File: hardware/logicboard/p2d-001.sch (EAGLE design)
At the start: 64 parts, among them IC1 74LS06N, IC2 4066N, IC3 MAX3468CPA, J1 MKR, J2 GPIO, J3 Vcc, J4 RLY, J5 SPI, K1 G5V1, T1 2SC1815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

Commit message: Fixed silk and wiring.
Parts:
- RN4: value (none) -> 220
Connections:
- removed net MI: IC1A.I, JP3.3, OK1A.VO1
- net MIN: now also IC1A.I, JP3.3, OK1A.VO1
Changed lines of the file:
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@@
 <part name="SUPPLY14" library="supply2" deviceset="GND" device=""/>
 <part name="IC1" library="74xx-us" library_urn="urn:adsk.eagle:library:88" deviceset="74*06" device="N" package3d_urn="urn:adsk.eagle:package:16407/2" technology="LS"/>
-<part name="RN4" library="resistor-dil" library_urn="urn:adsk.eagle:library:342" deviceset="8R-N" device="" package3d_urn="urn:adsk.eagle:package:922/2"/>
+<part name="RN4" library="resistor-dil" library_urn="urn:adsk.eagle:library:342" deviceset="8R-N" device="" package3d_urn="urn:adsk.eagle:package:922/2" value="220"/>
 <part name="D3" library="SparkFun-DiscreteSemi" library_urn="urn:adsk.eagle:library:514" deviceset="DIODE" device="-1N4148" package3d_urn="urn:adsk.eagle:package:38452/1" value=""/>
 <part name="RN2" library="resistor-net" library_urn="urn:adsk.eagle:library:343" deviceset="RN04" device="" package3d_urn="urn:adsk.eagle:package:24976/1" value="4.7k"/>
@@
 <label x="251.46" y="149.86" size="0.8128" layer="95" xref="yes"/>
 </segment>
+<segment>
+<pinref part="OK1" gate="A" pin="VO1"/>
+<wire x1="167.64" y1="119.38" x2="149.86" y2="119.38" width="0.1524" layer="91"/>
+<label x="147.32" y="119.38" size="0.8128" layer="95" rot="R180" xref="yes"/>
+<pinref part="IC1" gate="A" pin="I"/>
+<wire x1="149.86" y1="119.38" x2="147.32" y2="119.38" width="0.1524" layer="91"/>
+<wire x1="152.4" y1="101.6" x2="149.86" y2="101.6" width="0.1524" layer="91"/>
+<wire x1="149.86" y1="101.6" x2="149.86" y2="119.38" width="0.1524" layer="91"/>
+<junction x="149.86" y="119.38"/>
+</segment>
+<segment>
+<pinref part="JP3" gate="A" pin="3"/>
+<wire x1="132.08" y1="99.06" x2="142.24" y2="99.06" width="0.1524" layer="91"/>
+<label x="142.24" y="99.06" size="0.8128" layer="95" xref="yes"/>
+</segment>
 </net>
 <net name="NMTRTN" class="0">
@@
 </segment>
 </net>
-<net name="MI" class="0">
-<segment>
-<pinref part="OK1" gate="A" pin="VO1"/>
-<wire x1="167.64" y1="119.38" x2="149.86" y2="119.38" width="0.1524" layer="91"/>
-<label x="147.32" y="119.38" size="0.8128" layer="95" rot="R180" xref="yes"/>
-<pinref part="IC1" gate="A" pin="I"/>
-<wire x1="149.86" y1="119.38" x2="147.32" y2="119.38" width="0.1524" layer="91"/>
-<wire x1="152.4" y1="101.6" x2="149.86" y2="101.6" width="0.1524" layer="91"/>
-<wire x1="149.86" y1="101.6" x2="149.86" y2="119.38" width="0.1524" layer="91"/>
-<junction x="149.86" y="119.38"/>
-</segment>
-<segment>
-<pinref part="JP3" gate="A" pin="3"/>
-<wire x1="132.08" y1="99.06" x2="142.24" y2="99.06" width="0.1524" layer="91"/>
-<label x="142.24" y="99.06" size="0.8128" layer="95" xref="yes"/>
-</segment>
-</net>

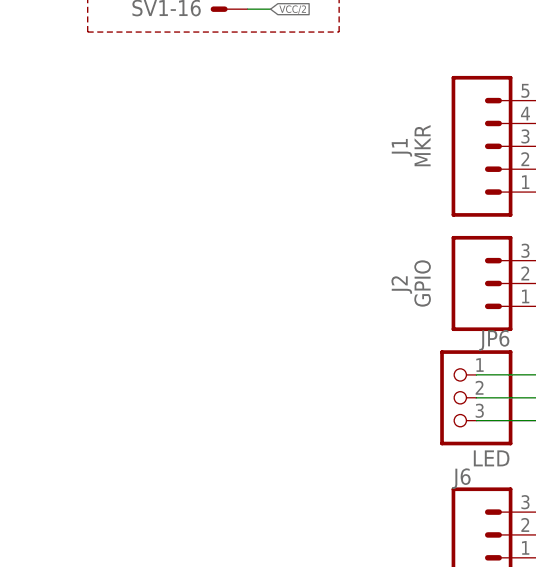
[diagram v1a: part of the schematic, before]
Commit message: Added J10 for external thermal sensor.
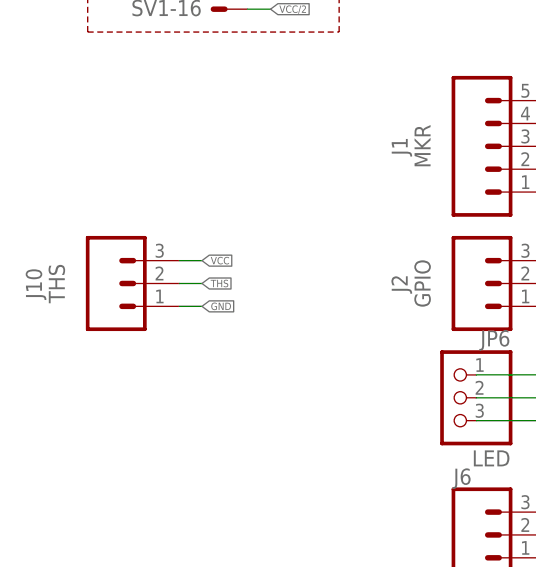
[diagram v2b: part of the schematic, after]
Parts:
- added J10: THS, SparkFun-Connectors:CONN_03JST-PTH
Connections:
- net GND: now also J10.1
- net THS: now also J10.2
- net VCC: now also J10.3
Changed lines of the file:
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@@
 <part name="A" library="wirepad" library_urn="urn:adsk.eagle:library:412" deviceset="SMD2" device="" package3d_urn="urn:adsk.eagle:package:30839/1"/>
 <part name="B" library="wirepad" library_urn="urn:adsk.eagle:library:412" deviceset="SMD2" device="" package3d_urn="urn:adsk.eagle:package:30839/1"/>
+<part name="J10" library="SparkFun-Connectors" library_urn="urn:adsk.eagle:library:513" deviceset="CONN_03" device="JST-PTH" package3d_urn="urn:adsk.eagle:package:38069/1" value="THS"/>
 </parts>
 <sheets>
@@
 <attribute name="NAME" x="109.22" y="218.44" size="1.778" layer="95" align="bottom-center"/>
 <attribute name="VALUE" x="105.918" y="217.043" size="1.778" layer="96" rot="R270"/>
+</instance>
+<instance part="J10" gate="J$1" x="25.4" y="48.26" smashed="yes">
+<attribute name="VALUE" x="20.32" y="48.26" size="1.778" layer="96" rot="R90" align="bottom-center"/>
+<attribute name="NAME" x="17.78" y="48.26" size="1.778" layer="95" rot="R90" align="bottom-center"/>
 </instance>
 </instances>
@@
 <label x="314.96" y="203.2" size="0.8128" layer="95" rot="R180" xref="yes"/>
 </segment>
+<segment>
+<pinref part="J10" gate="J$1" pin="1"/>
+<wire x1="33.02" y1="45.72" x2="35.56" y2="45.72" width="0.1524" layer="91"/>
+<label x="35.56" y="45.72" size="0.8128" layer="95" xref="yes"/>
+</segment>
 </net>
 <net name="VCC" class="2">
@@
 <label x="314.96" y="193.04" size="0.8128" layer="95" rot="R180" xref="yes"/>
 </segment>
+<segment>
+<pinref part="J10" gate="J$1" pin="3"/>
+<wire x1="33.02" y1="50.8" x2="35.56" y2="50.8" width="0.1524" layer="91"/>
+<label x="35.56" y="50.8" size="0.8128" layer="95" xref="yes"/>
+</segment>
 </net>
 <net name="RLYSNK" class="0">
@@
 <label x="337.82" y="193.04" size="0.8128" layer="95" xref="yes"/>
 </segment>
+<segment>
+<pinref part="J10" gate="J$1" pin="2"/>
+<wire x1="33.02" y1="48.26" x2="35.56" y2="48.26" width="0.1524" layer="91"/>
+<label x="35.56" y="48.26" size="0.8128" layer="95" xref="yes"/>
+</segment>
 </net>

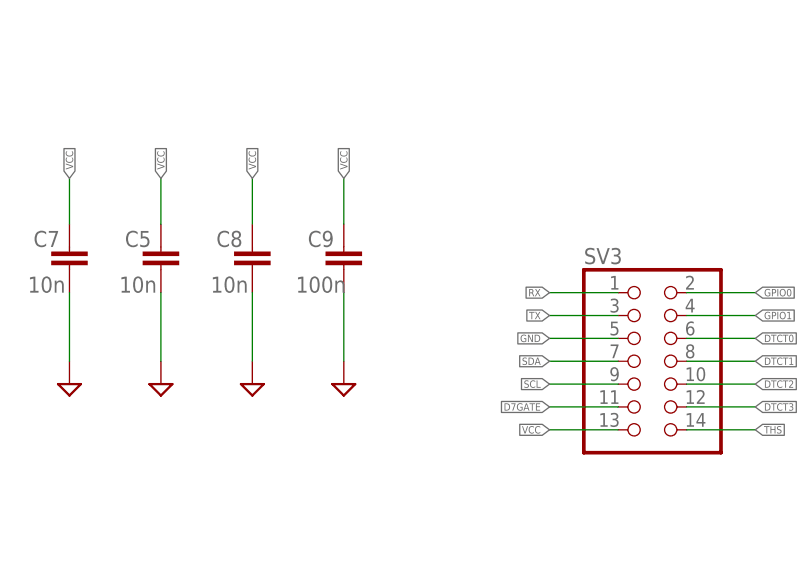
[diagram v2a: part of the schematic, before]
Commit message: Added C11.
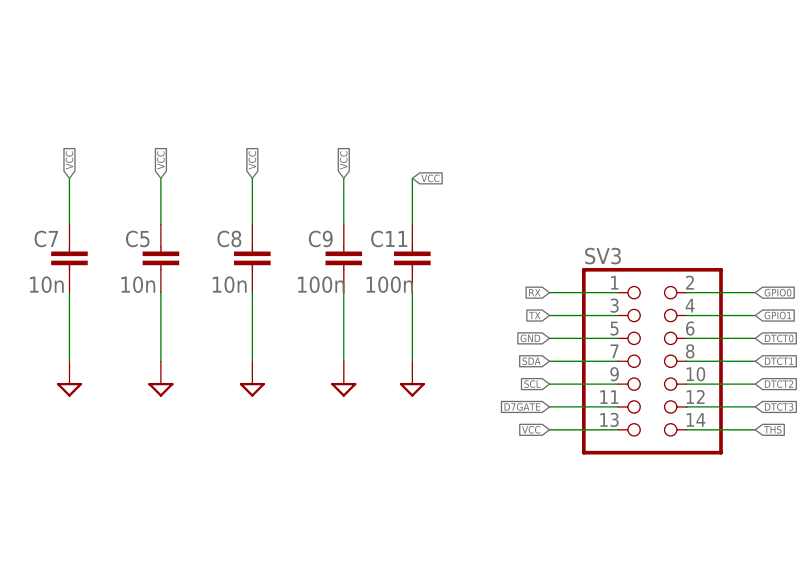
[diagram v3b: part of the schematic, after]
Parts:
- added C11: 100n, resistor:C-EU025-024X044
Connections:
- net GND: now also C11.2
- net VCC: now also C11.1
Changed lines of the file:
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@@
 <part name="B" library="wirepad" library_urn="urn:adsk.eagle:library:412" deviceset="SMD2" device="" package3d_urn="urn:adsk.eagle:package:30839/1"/>
 <part name="J10" library="SparkFun-Connectors" library_urn="urn:adsk.eagle:library:513" deviceset="CONN_03" device="JST-PTH" package3d_urn="urn:adsk.eagle:package:38069/1" value="THS"/>
+<part name="C11" library="resistor" library_urn="urn:adsk.eagle:library:348" deviceset="C-EU" device="025-024X044" package3d_urn="urn:adsk.eagle:package:23630/1" value="100n"/>
+<part name="SUPPLY8" library="supply2" deviceset="GND" device=""/>
 </parts>
 <sheets>
@@
 <attribute name="NAME" x="17.78" y="48.26" size="1.778" layer="95" rot="R90" align="bottom-center"/>
 </instance>
+<instance part="C11" gate="G$1" x="299.72" y="213.36" smashed="yes">
+<attribute name="NAME" x="297.18" y="213.36" size="1.778" layer="95" align="bottom-center"/>
+<attribute name="VALUE" x="297.18" y="208.28" size="1.778" layer="96" align="bottom-center"/>
+</instance>
+<instance part="SUPPLY8" gate="GND" x="299.72" y="198.12" smashed="yes"/>
 </instances>
 <busses>
@@
 <label x="35.56" y="45.72" size="0.8128" layer="95" xref="yes"/>
 </segment>
+<segment>
+<pinref part="C11" gate="G$1" pin="2"/>
+<pinref part="SUPPLY8" gate="GND" pin="GND"/>
+<wire x1="299.72" y1="208.28" x2="299.72" y2="200.66" width="0.1524" layer="91"/>
+</segment>
 </net>
 <net name="VCC" class="2">
@@
 <label x="35.56" y="50.8" size="0.8128" layer="95" xref="yes"/>
 </segment>
+<segment>
+<pinref part="C11" gate="G$1" pin="1"/>
+<wire x1="299.72" y1="215.9" x2="299.72" y2="220.98" width="0.1524" layer="91"/>
+<label x="299.72" y="220.98" size="0.8128" layer="95" xref="yes"/>
+</segment>
 </net>

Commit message: New TestPort II.
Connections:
- net DTCT0: now also SV3.8; no longer SV3.6
- net DTCT1: now also SV3.10; no longer SV3.8
- net DTCT2: now also SV3.12; no longer SV3.10
- net DTCT3: now also SV3.14; no longer SV3.12
- net RX: now also SV3.3; no longer SV3.1
- net THS: now also SV3.6; no longer SV3.14
- net TX: now also SV3.1; no longer SV3.3
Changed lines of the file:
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@@
-</segment>
-<segment>
-<pinref part="SV3" gate="A" pin="14"/>
-<wire x1="330.2" y1="193.04" x2="337.82" y2="193.04" width="0.1524" layer="91"/>
-<label x="337.82" y="193.04" size="0.8128" layer="95" xref="yes"/>
 </segment>
 <segment>
@@
 <wire x1="33.02" y1="48.26" x2="35.56" y2="48.26" width="0.1524" layer="91"/>
 <label x="35.56" y="48.26" size="0.8128" layer="95" xref="yes"/>
+</segment>
+<segment>
+<pinref part="SV3" gate="A" pin="6"/>
+<wire x1="330.2" y1="203.2" x2="337.82" y2="203.2" width="0.1524" layer="91"/>
+<label x="337.82" y="203.2" size="0.8128" layer="95" xref="yes"/>
 </segment>
 </net>
@@
 </segment>
 <segment>
-<pinref part="SV3" gate="A" pin="3"/>
-<wire x1="322.58" y1="205.74" x2="314.96" y2="205.74" width="0.1524" layer="91"/>
-<label x="314.96" y="205.74" size="0.8128" layer="95" rot="R180" xref="yes"/>
+<pinref part="SV3" gate="A" pin="1"/>
+<wire x1="322.58" y1="208.28" x2="314.96" y2="208.28" width="0.1524" layer="91"/>
+<label x="314.96" y="208.28" size="0.8128" layer="95" rot="R180" xref="yes"/>
 </segment>
 </net>
@@
 </segment>
 <segment>
-<pinref part="SV3" gate="A" pin="1"/>
-<wire x1="322.58" y1="208.28" x2="314.96" y2="208.28" width="0.1524" layer="91"/>
-<label x="314.96" y="208.28" size="0.8128" layer="95" rot="R180" xref="yes"/>
+<pinref part="SV3" gate="A" pin="3"/>
+<wire x1="322.58" y1="205.74" x2="314.96" y2="205.74" width="0.1524" layer="91"/>
+<label x="314.96" y="205.74" size="0.8128" layer="95" rot="R180" xref="yes"/>
 </segment>
 </net>
@@
 </segment>
 <segment>
-<pinref part="SV3" gate="A" pin="6"/>
-<wire x1="330.2" y1="203.2" x2="337.82" y2="203.2" width="0.1524" layer="91"/>
-<label x="337.82" y="203.2" size="0.8128" layer="95" xref="yes"/>
+<pinref part="SV3" gate="A" pin="8"/>
+<wire x1="330.2" y1="200.66" x2="337.82" y2="200.66" width="0.1524" layer="91"/>
+<label x="337.82" y="200.66" size="0.8128" layer="95" xref="yes"/>
 </segment>
 </net>
@@
 </segment>
 <segment>
-<pinref part="SV3" gate="A" pin="8"/>
-<wire x1="330.2" y1="200.66" x2="337.82" y2="200.66" width="0.1524" layer="91"/>
-<label x="337.82" y="200.66" size="0.8128" layer="95" xref="yes"/>
+<pinref part="SV3" gate="A" pin="10"/>
+<wire x1="330.2" y1="198.12" x2="337.82" y2="198.12" width="0.1524" layer="91"/>
+<label x="337.82" y="198.12" size="0.8128" layer="95" xref="yes"/>
 </segment>
 </net>
@@
 </segment>
 <segment>
-<pinref part="SV3" gate="A" pin="10"/>
-<wire x1="330.2" y1="198.12" x2="337.82" y2="198.12" width="0.1524" layer="91"/>
-<label x="337.82" y="198.12" size="0.8128" layer="95" xref="yes"/>
+<pinref part="SV3" gate="A" pin="12"/>
+<wire x1="330.2" y1="195.58" x2="337.82" y2="195.58" width="0.1524" layer="91"/>
+<label x="337.82" y="195.58" size="0.8128" layer="95" xref="yes"/>
 </segment>
 </net>
@@
 </segment>
 <segment>
-<pinref part="SV3" gate="A" pin="12"/>
-<wire x1="330.2" y1="195.58" x2="337.82" y2="195.58" width="0.1524" layer="91"/>
-<label x="337.82" y="195.58" size="0.8128" layer="95" xref="yes"/>
-</segment>
-</net>
+<pinref part="SV3" gate="A" pin="14"/>
+<wire x1="330.2" y1="193.04" x2="337.82" y2="193.04" width="0.1524" layer="91"/>
+<label x="337.82" y="193.04" size="0.8128" layer="95" xref="yes"/>
+</segment>
+</net>

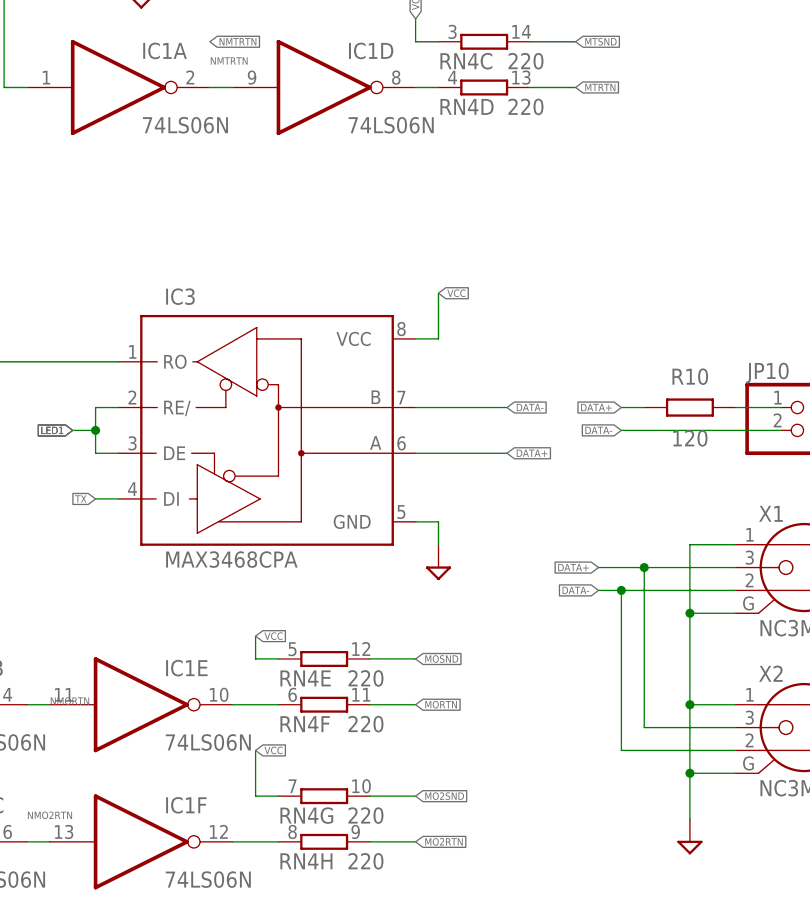
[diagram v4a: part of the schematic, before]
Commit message: Added pull-up R to DMX signals.
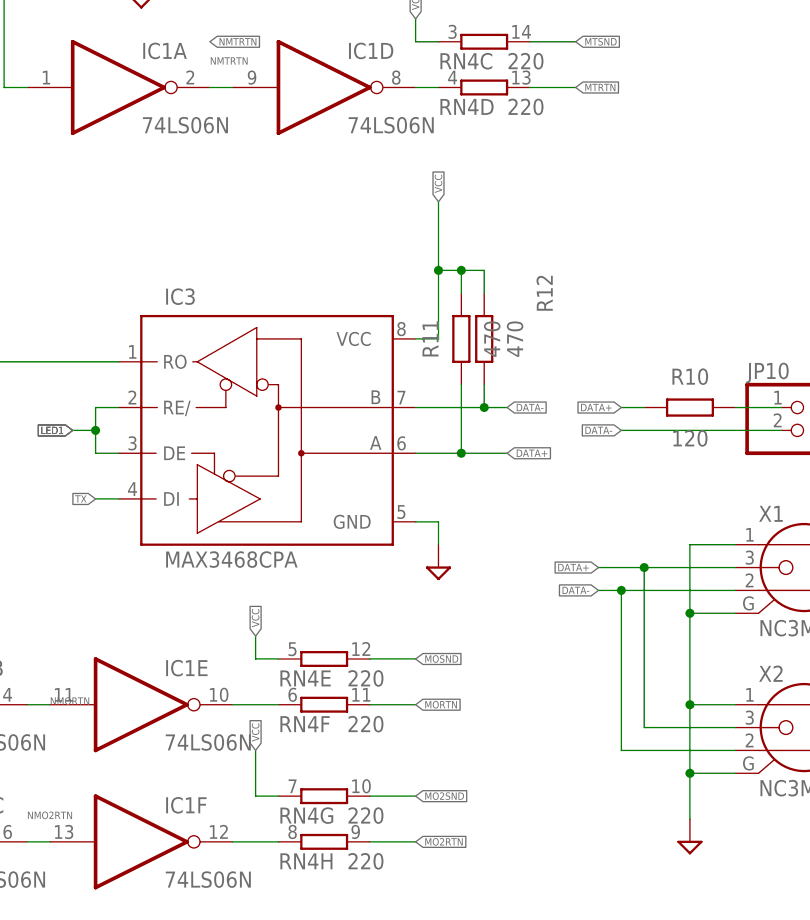
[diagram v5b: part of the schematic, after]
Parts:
- added R11, R12: 470, resistor:R-EU_0204/5
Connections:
- net DATA+: now also R11.1
- net DATA-: now also R12.1
- net VCC: now also R11.2, R12.2
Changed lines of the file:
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@@
 <part name="C11" library="resistor" library_urn="urn:adsk.eagle:library:348" deviceset="C-EU" device="025-024X044" package3d_urn="urn:adsk.eagle:package:23630/1" value="100n"/>
 <part name="SUPPLY8" library="supply2" deviceset="GND" device=""/>
+<part name="R11" library="resistor" library_urn="urn:adsk.eagle:library:348" deviceset="R-EU_" device="0204/5" package3d_urn="urn:adsk.eagle:package:23488/1" value="470"/>
+<part name="R12" library="resistor" library_urn="urn:adsk.eagle:library:348" deviceset="R-EU_" device="0204/5" package3d_urn="urn:adsk.eagle:package:23488/1" value="470"/>
 </parts>
 <sheets>
@@
 </instance>
 <instance part="SUPPLY8" gate="GND" x="299.72" y="198.12" smashed="yes"/>
+<instance part="R11" gate="G$1" x="200.66" y="73.66" smashed="yes" rot="R90">
+<attribute name="NAME" x="198.12" y="73.66" size="1.778" layer="95" rot="R90" align="bottom-center"/>
+<attribute name="VALUE" x="203.2" y="73.66" size="1.778" layer="96" rot="R90" align="top-center"/>
+</instance>
+<instance part="R12" gate="G$1" x="203.2" y="73.66" smashed="yes" rot="R90">
+<attribute name="NAME" x="210.82" y="78.74" size="1.778" layer="95" rot="R90" align="bottom-center"/>
+<attribute name="VALUE" x="205.74" y="73.66" size="1.778" layer="96" rot="R90" align="top-center"/>
+</instance>
 </instances>
 <busses>
@@
 <pinref part="IC3" gate="G$1" pin="VCC"/>
 <wire x1="195.58" y1="73.66" x2="198.12" y2="73.66" width="0.1524" layer="91"/>
-<wire x1="198.12" y1="73.66" x2="198.12" y2="78.74" width="0.1524" layer="91"/>
-<label x="198.12" y="78.74" size="0.8128" layer="95" xref="yes"/>
+<wire x1="198.12" y1="73.66" x2="198.12" y2="81.28" width="0.1524" layer="91"/>
+<label x="198.12" y="88.9" size="0.8128" layer="95" rot="R90" xref="yes"/>
+<pinref part="R11" gate="G$1" pin="2"/>
+<wire x1="198.12" y1="81.28" x2="198.12" y2="88.9" width="0.1524" layer="91"/>
+<wire x1="200.66" y1="78.74" x2="200.66" y2="81.28" width="0.1524" layer="91"/>
+<wire x1="200.66" y1="81.28" x2="198.12" y2="81.28" width="0.1524" layer="91"/>
+<junction x="198.12" y="81.28"/>
+<pinref part="R12" gate="G$1" pin="2"/>
+<wire x1="203.2" y1="78.74" x2="203.2" y2="81.28" width="0.1524" layer="91"/>
+<wire x1="203.2" y1="81.28" x2="200.66" y2="81.28" width="0.1524" layer="91"/>
+<junction x="200.66" y="81.28"/>
 </segment>
 <segment>
@@
 <wire x1="180.34" y1="38.1" x2="177.8" y2="38.1" width="0.1524" layer="91"/>
 <wire x1="177.8" y1="38.1" x2="177.8" y2="40.64" width="0.1524" layer="91"/>
-<label x="177.8" y="40.64" size="0.8128" layer="95" xref="yes"/>
+<label x="177.8" y="40.64" size="0.8128" layer="95" rot="R90" xref="yes"/>
 </segment>
 <segment>
@@
 <wire x1="180.34" y1="22.86" x2="177.8" y2="22.86" width="0.1524" layer="91"/>
 <wire x1="177.8" y1="22.86" x2="177.8" y2="27.94" width="0.1524" layer="91"/>
-<label x="177.8" y="27.94" size="0.8128" layer="95" xref="yes"/>
+<label x="177.8" y="27.94" size="0.8128" layer="95" rot="R90" xref="yes"/>
 </segment>
 <segment>
@@
 <net name="DATA+" class="0">
 <segment>
-<pinref part="IC3" gate="G$1" pin="A"/>
-<wire x1="195.58" y1="60.96" x2="205.74" y2="60.96" width="0.1524" layer="91"/>
-<label x="205.74" y="60.96" size="0.8128" layer="95" xref="yes"/>
-</segment>
-<segment>
 <pinref part="R10" gate="G$1" pin="1"/>
 <wire x1="220.98" y1="66.04" x2="218.44" y2="66.04" width="0.1524" layer="91"/>
@@
 <label x="215.9" y="48.26" size="0.8128" layer="95" rot="R180" xref="yes"/>
 </segment>
+<segment>
+<pinref part="IC3" gate="G$1" pin="A"/>
+<label x="205.74" y="60.96" size="0.8128" layer="95" xref="yes"/>
+<wire x1="195.58" y1="60.96" x2="200.66" y2="60.96" width="0.1524" layer="91"/>
+<pinref part="R11" gate="G$1" pin="1"/>
+<wire x1="200.66" y1="60.96" x2="205.74" y2="60.96" width="0.1524" layer="91"/>
+<wire x1="200.66" y1="68.58" x2="200.66" y2="60.96" width="0.1524" layer="91"/>
+<junction x="200.66" y="60.96"/>
+</segment>
 </net>
 <net name="DATA-" class="0">
-<segment>
-<pinref part="IC3" gate="G$1" pin="B"/>
-<wire x1="195.58" y1="66.04" x2="205.74" y2="66.04" width="0.1524" layer="91"/>
-<label x="205.74" y="66.04" size="0.8128" layer="95" xref="yes"/>
-</segment>
 <segment>
 <pinref part="JP10" gate="G$1" pin="2"/>
@@
 <label x="215.9" y="45.72" size="0.8128" layer="95" rot="R180" xref="yes"/>
 </segment>
-</net>
+<segment>
+<pinref part="IC3" gate="G$1" pin="B"/>
+<wire x1="195.58" y1="66.04" x2="203.2" y2="66.04" width="0.1524" layer="91"/>
+<label x="205.74" y="66.04" size="0.8128" layer="95" xref="yes"/>
+<pinref part="R12" gate="G$1" pin="1"/>
+<wire x1="203.2" y1="66.04" x2="205.74" y2="66.04" width="0.1524" layer="91"/>
+<wire x1="203.2" y1="68.58" x2="203.2" y2="66.04" width="0.1524" layer="91"/>
+<junction x="203.2" y="66.04"/>
+</segment>
+</net>

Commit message: Cleaning up.
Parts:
- J6: value (none) -> LED
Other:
- moved on the sheet: C11, C5, C6, C7, C8, C9, D3, DMXRX, IC1A, IC1D, J1, J10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

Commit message: Clean up.
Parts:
- JP10: value (none) -> SelfTerminate
- JP3: value (none) -> RXSelect
- SV2: value (none) -> Backport II
- SV3: value (none) -> Testport II
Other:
- moved on the sheet: C10, IC1B, IC1C, IC1E, IC1F, IC3, JP10, OK1B, R10, R11, R12, R3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
